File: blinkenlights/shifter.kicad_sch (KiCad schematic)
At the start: 43 parts, among them U601 SN74LVCH16T245, U602 SN74LXC8T245, U603 SN74LVC2T45, U604 SN74LVC2T45, U605 SN74LVC2T45, U606 SN74LVCH16T245, U607 SN74LXC8T245, U608 74LVC2G06, U609 74LVC2G06, U610 74LVC2G06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

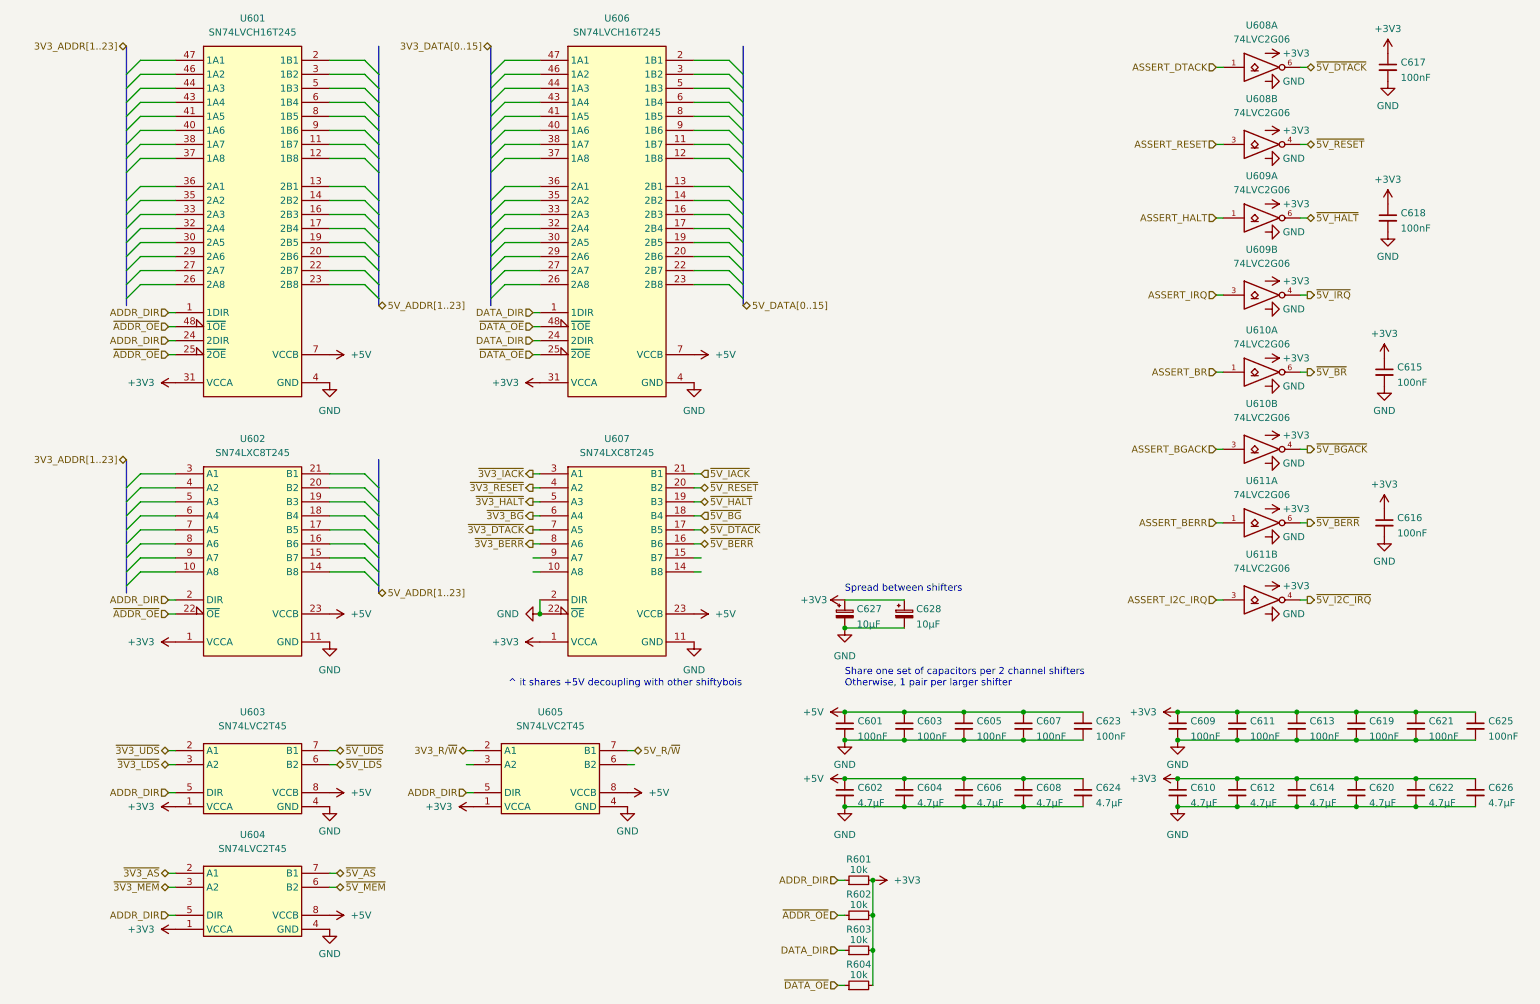
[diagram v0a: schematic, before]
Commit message: Get rid of CPU on blinkenlights board
- We don't really care for having a full processor chilling on this
  board more than we do about being able to do a few bus transactions
  (to do fun stuff like flashing the boot ROMs) so we're going to put a
  bunch of SPI IO expanders instead; this should allow us to somewhat
  recreate bus cycles.

  We'll have to implement the run/halt/single step controls with
  dedicated logic though.
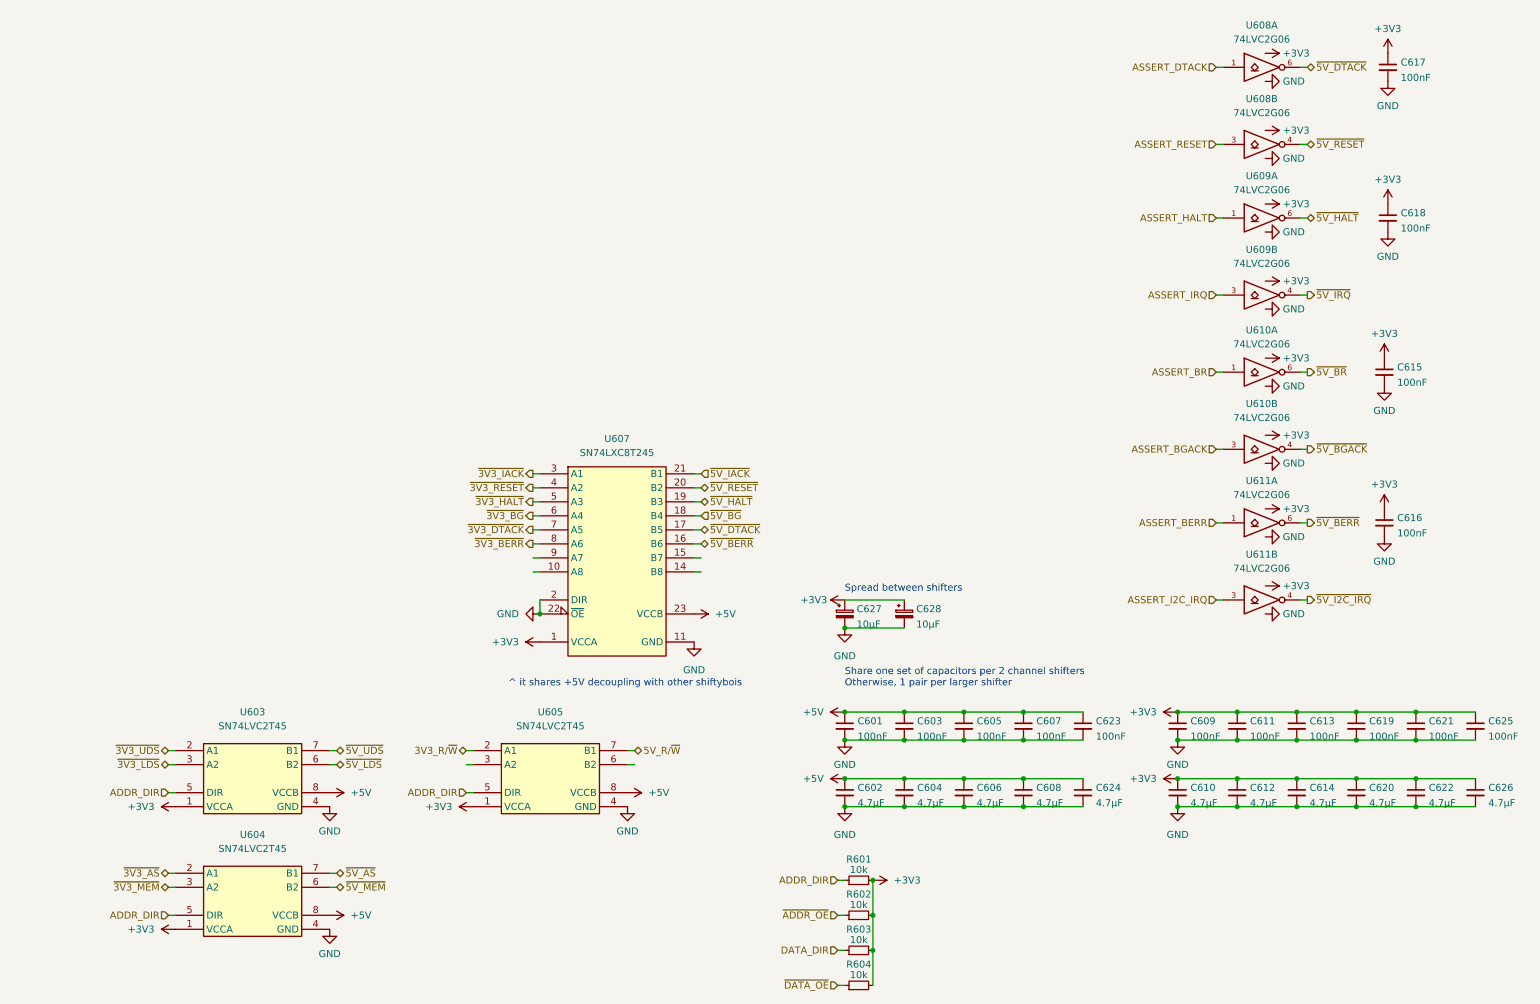
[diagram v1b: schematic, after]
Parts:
- removed U601, U606: SN74LVCH16T245, Package_SO:TSSOP-48_6.1x12.5mm_P0.5mm, symbol 68komputer-common:SN74LVCH16T245
- removed U602: SN74LXC8T245, Package_SO:TSSOP-24_4.4x7.8mm_P0.65mm, symbol 68komputer-common:SN74LXC8T245

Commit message: Connected data/address bus to expanders
- Finished routing the remaining address and data lines to the SPI IO
  expanders, which are used externally to control the bus. Also removed
  some superfluous level shifters
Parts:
- removed C605, C607, C613, C619, C621, C623, C625: 100nF, Capacitor_SMD:C_0805_2012Metric, symbol Device:C_Small
- removed C606, C608, C614, C620, C622, C624, C626: 4.7µF, Capacitor_SMD:C_0805_2012Metric, symbol Device:C_Small

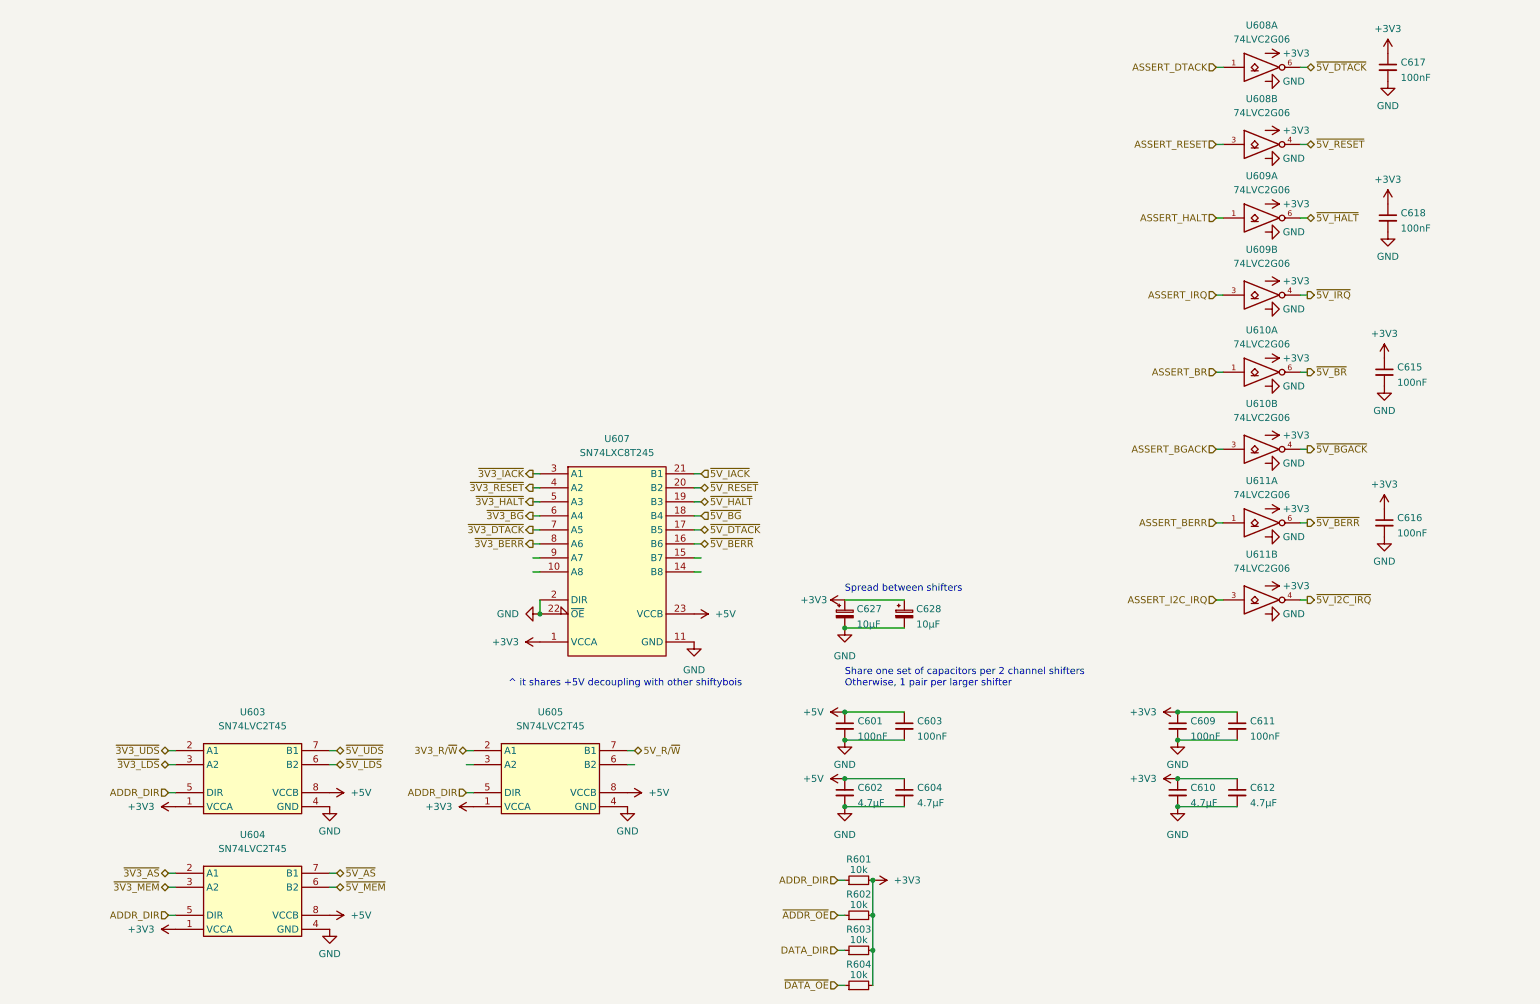
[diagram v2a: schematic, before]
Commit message: Routed control signals
- The blinkenlights board now has the control signals routed to IO
  expanders, and removed a bunch of superfluous level shifting type
  stuff
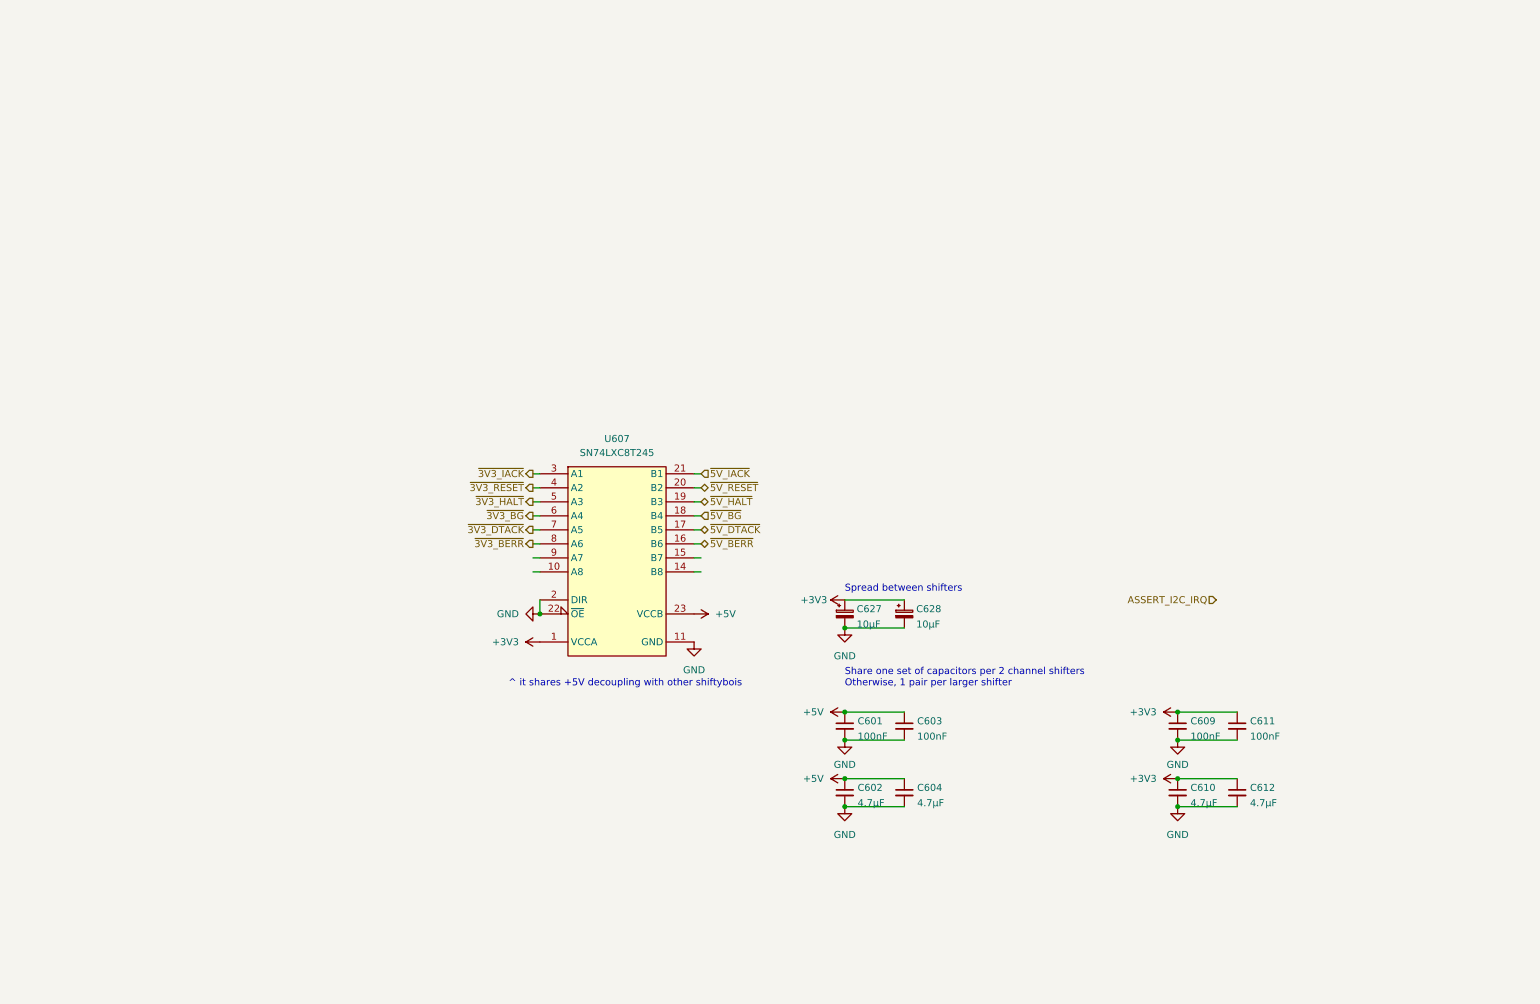
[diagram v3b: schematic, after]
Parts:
- removed C615, C616, C617, C618: 100nF, Capacitor_SMD:C_0805_2012Metric, symbol Device:C_Small
- removed R601, R602, R603, R604: 10k, Resistor_SMD:R_0805_2012Metric, symbol Device:R_Small
- removed U603, U604, U605: SN74LVC2T45, Package_SO:VSSOP-8_2.3x2mm_P0.5mm, symbol 68komputer-common:SN74LVC2T45
- removed U608, U611: 74LVC2G06, Package_TO_SOT_SMD:SOT-23-6, symbol 74xGxx:74LVC2G06
- removed U609, U610: 74LVC2G06, symbol 74xGxx:74LVC2G06
